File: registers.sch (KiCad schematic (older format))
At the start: 18 parts

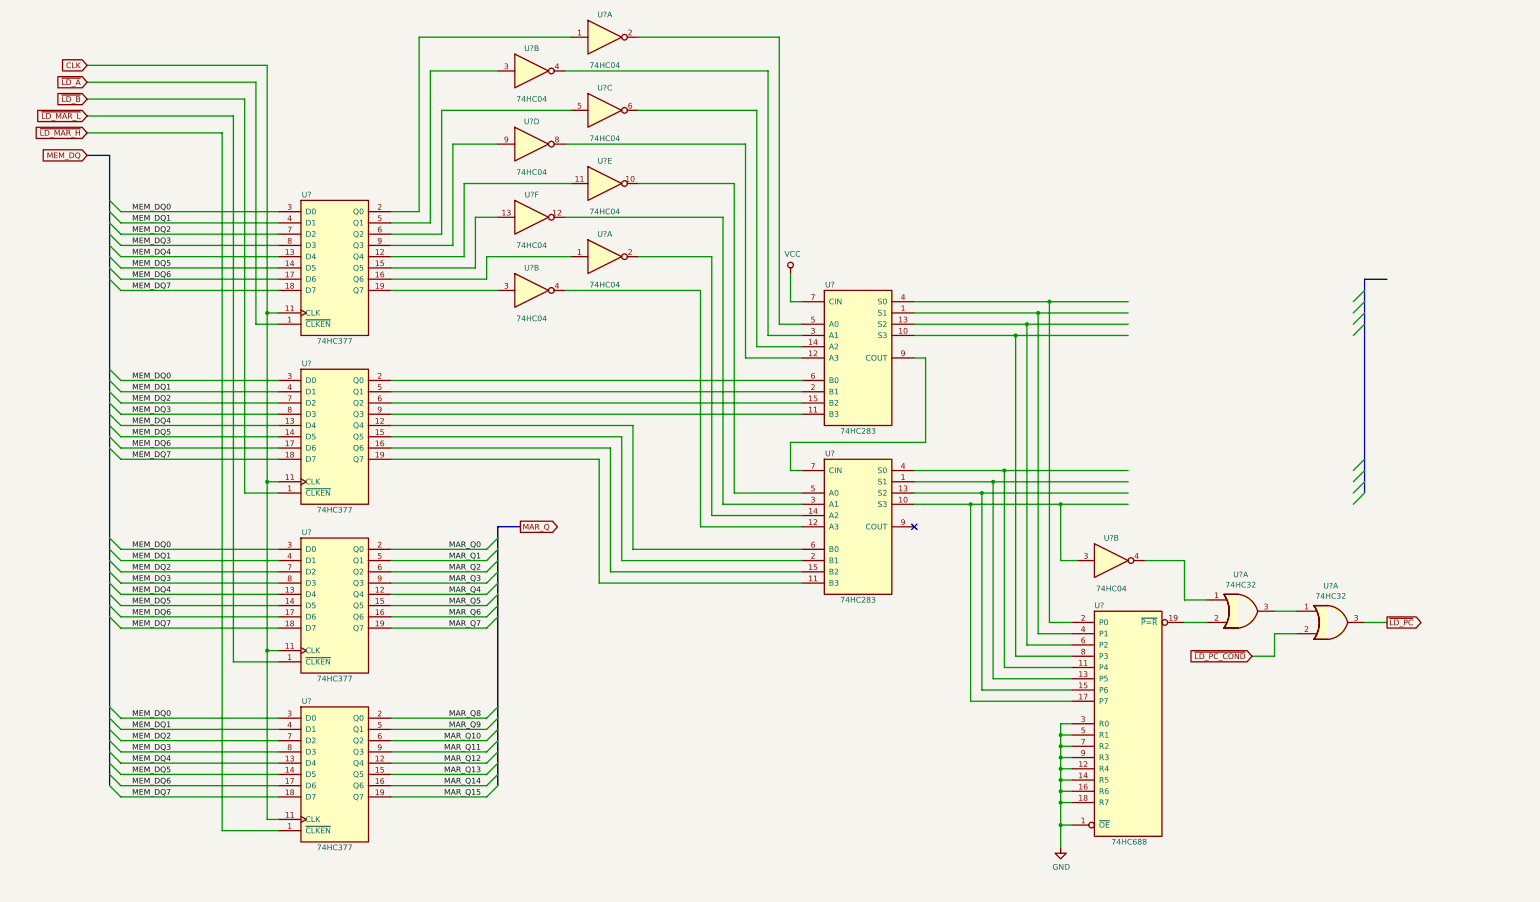
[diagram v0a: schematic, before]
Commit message: finished ALU and registers
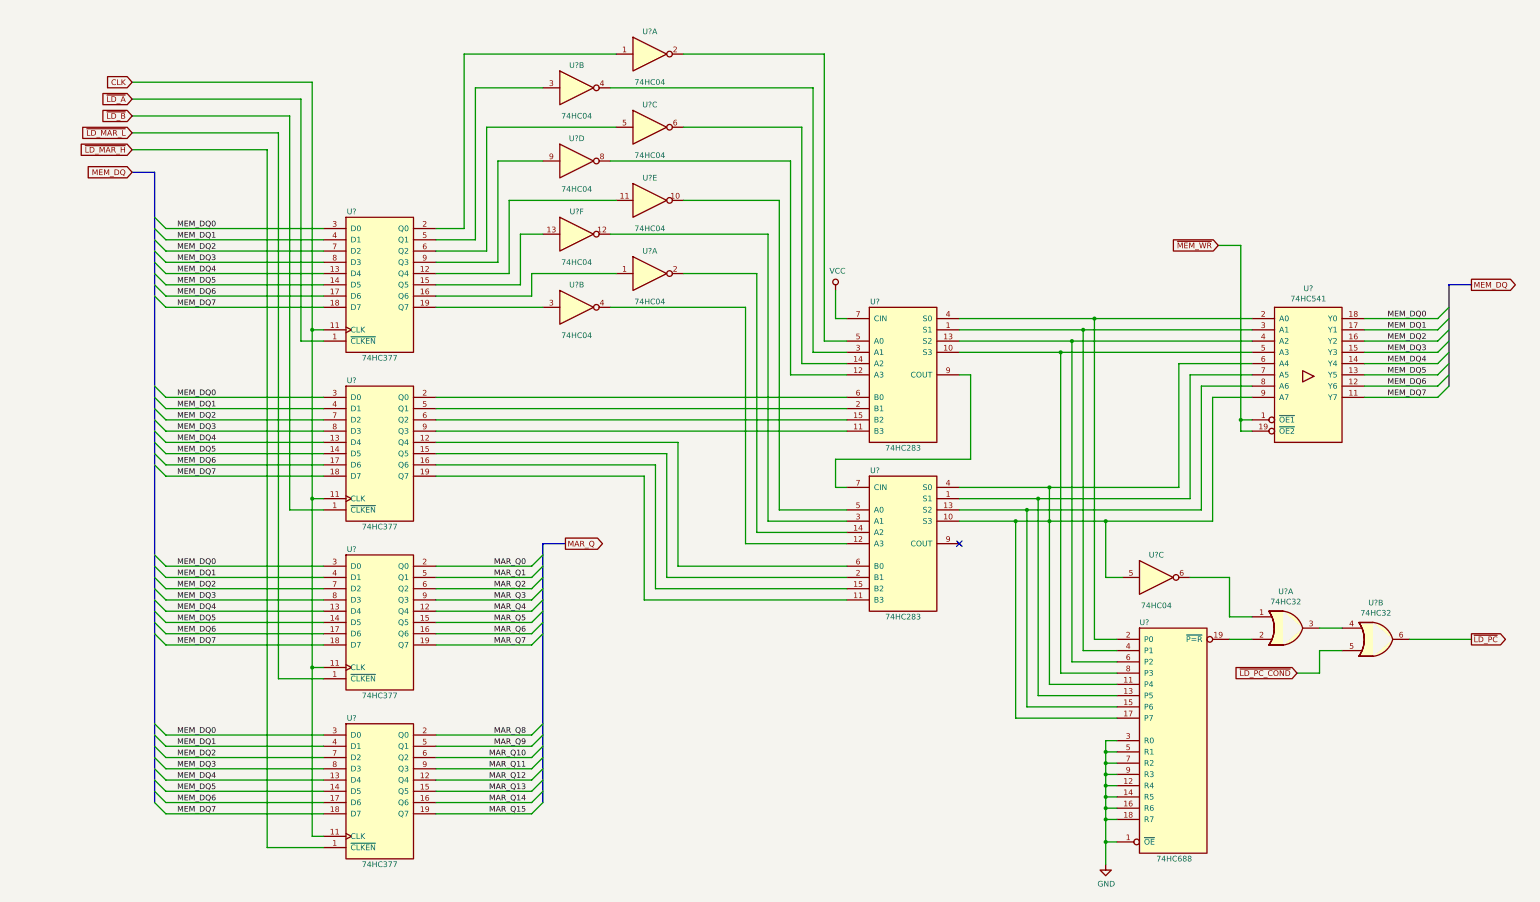
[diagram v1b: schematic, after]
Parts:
- added U?: 74HC541, symbol 74xx_modified:74LS541
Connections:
- net labels added: ~MEM_WR
- wire segments 200 -> 223
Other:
- moved on the sheet: U?, U?A, U?B, U?C, U?D, U?E, U?F

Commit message: backup before registers alu split
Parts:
- removed U? (x4): 74HC377, symbol 74xx_modified:74LS377
- removed U? (x2): 74HC283, symbol 74xx_modified:74LS283
- removed U? (x9): 74HC04, Package_DIP:DIP-14_W7.62mm, symbol 74xx:74LS04
- removed U?: 74HC688, symbol 74xx_modified:74LS688
- removed U? (x2): 74HC32, symbol 74xx_modified:74LS32
- removed U?: 74HC541, symbol 74xx_modified:74LS541
- added U? (x4): 74HC377, symbol 74xx_modified:74LS377
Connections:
- net CLK: now also U?.11 (CLK), U?.11 (CLK), U?.11 (CLK), U?.11 (CLK)
- net GND: now also U?.10 (GND), U?.10 (GND), U?.10 (GND), U?.10 (GND)
- net MAR_Q0: now also U?.2 (Q0)
- net MAR_Q1: now also U?.5 (Q1)
- net MAR_Q10: now also U?.6 (Q2)
- net MAR_Q11: now also U?.9 (Q3)
- net MAR_Q12: now also U?.12 (Q4)
- net MAR_Q13: now also U?.15 (Q5)
- net MAR_Q14: now also U?.16 (Q6)
- net MAR_Q15: now also U?.19 (Q7)
- net MAR_Q2: now also U?.6 (Q2)
- net MAR_Q3: now also U?.9 (Q3)
- net MAR_Q4: now also U?.12 (Q4)
- net MAR_Q5: now also U?.15 (Q5)
- net MAR_Q6: now also U?.16 (Q6)
- net MAR_Q7: now also U?.19 (Q7)
- net MAR_Q8: now also U?.2 (Q0)
- net MAR_Q9: now also U?.5 (Q1)
- net MEM_DQ0: now also U?.3 (D0), U?.3 (D0), U?.3 (D0), U?.3 (D0)
- net MEM_DQ1: now also U?.4 (D1), U?.4 (D1), U?.4 (D1), U?.4 (D1)
- net MEM_DQ2: now also U?.7 (D2), U?.7 (D2), U?.7 (D2), U?.7 (D2)
- net MEM_DQ3: now also U?.8 (D3), U?.8 (D3), U?.8 (D3), U?.8 (D3)
- net MEM_DQ4: now also U?.13 (D4), U?.13 (D4), U?.13 (D4), U?.13 (D4)
- net MEM_DQ5: now also U?.14 (D5), U?.14 (D5), U?.14 (D5), U?.14 (D5)
- net MEM_DQ6: now also U?.17 (D6), U?.17 (D6), U?.17 (D6), U?.17 (D6)
- net MEM_DQ7: now also U?.18 (D7), U?.18 (D7), U?.18 (D7), U?.18 (D7)
- net VCC: now also U?.20 (VCC), U?.20 (VCC), U?.20 (VCC), U?.20 (VCC)
- net ~LD_A: now also U?.1 (~CLKEN)
- net ~LD_B: now also U?.1 (~CLKEN)
- net ~LD_MAR_H: now also U?.1 (~CLKEN)
- net ~LD_MAR_L: now also U?.1 (~CLKEN)
- no-connect marks 1 -> 0
